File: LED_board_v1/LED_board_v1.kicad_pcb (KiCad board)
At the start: 2 copper layers, 100 x 68 mm, 45 parts, among them J1 Conn_01x03_Pin, J10 Conn_01x03_Pin, J11 Conn_01x03_Pin, J12 Conn_01x02_Pin, J2 Conn_ST_STDC14, J3 Conn_01x03_Pin, J4 Conn_01x03_Pin, J5 Conn_01x03_Pin, J6 Conn_01x03_Pin, J7 Conn_01x03_Pin, J8 Conn_01x03_Pin, J9 Conn_01x03_Pin, SW1 SW_Push, SW2 SW_SPDT, U1 PTCAN3414DDFR, U2 STM32H533CETx, U3 NID60S48-24, U4 BD33FC0FP, U5 74AHCT125, U6 74AHCT125

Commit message: md改良(ちょっと前にしたやつ上げ忘れ)
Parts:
- added D1: LED, LED_SMD:LED_0805_2012Metric_Pad1.15x1.40mm_HandSolder, F.Cu at (105.2, 83.4)
- added D3: LED, LED_SMD:LED_0805_2012Metric_Pad1.15x1.40mm_HandSolder, F.Cu at (109.1, 83.4)
- added R3: 1k, Resistor_SMD:R_0603_1608Metric_Pad0.98x0.95mm_HandSolder, B.Cu at (105.3, 83.4)
- added R4: 1k, Resistor_SMD:R_0603_1608Metric_Pad0.98x0.95mm_HandSolder, B.Cu at (109.1, 83.4)
- moved C14 0.78 mm to (99.5, 84.9)
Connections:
- U2 pad 25: unconnected-(U2-PB12-Pad25) -> Net-(D1-A)
- U2 pad 26: unconnected-(U2-PB13-Pad26) -> Net-(D3-A)
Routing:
- net Net-(D3-A): track 0.00 -> 9.68 mm
- net GND: track 23.0 -> 31.1 mm, vias 68 -> 138
- net Net-(D1-A): track 0.00 -> 5.66 mm
- net nrst: track 36.4 -> 38.6 mm
- net +3.3V: track 87.1 -> 86.6 mm
- net Net-(D3-K): track 0.00 -> 0.13 mm, vias 0 -> 1
- net Net-(D1-K): track 0.00 -> 0.05 mm, vias 0 -> 1
- net /can_-: vias 1 -> 2

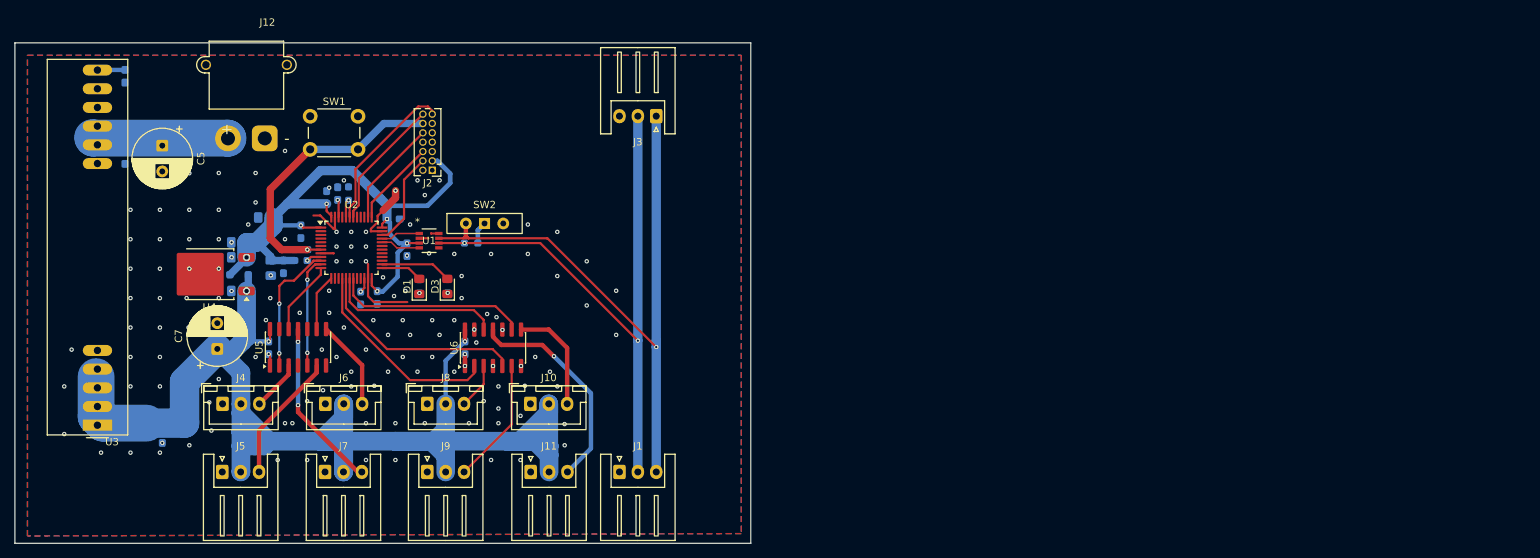
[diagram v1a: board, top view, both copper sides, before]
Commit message: MDPID基板を作ったりLED基板の電源回りをいじった
MDPIDの電源変更+配線
LED基板の電源変更(未配線)
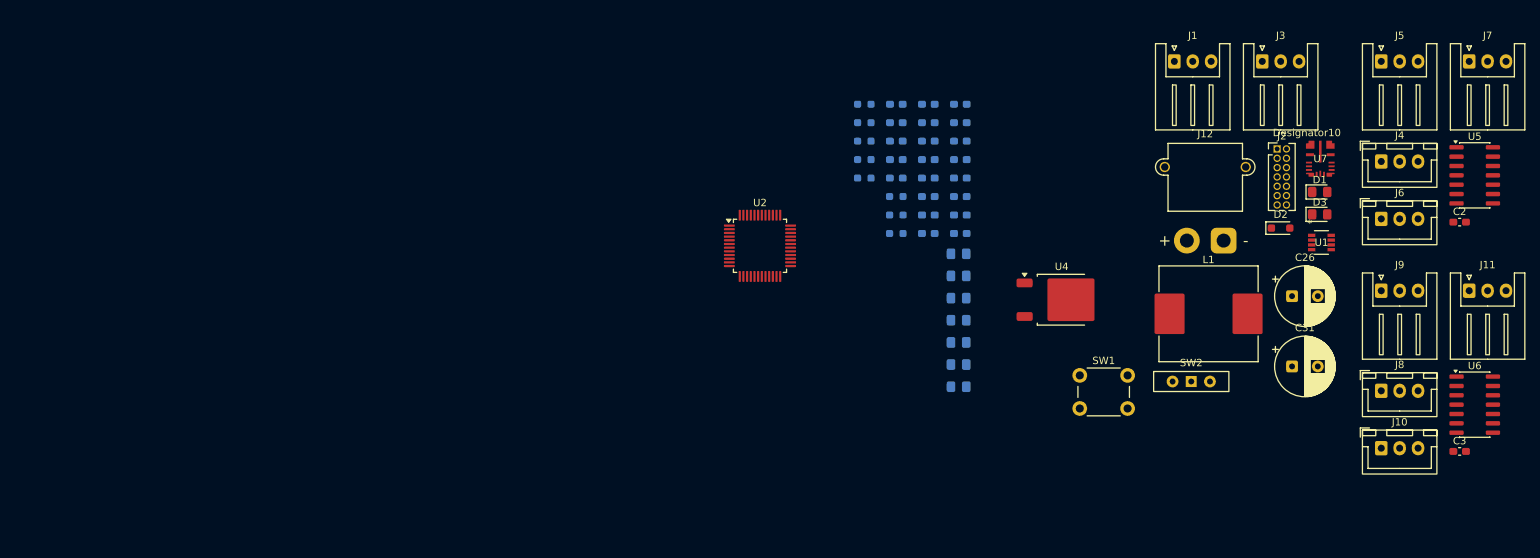
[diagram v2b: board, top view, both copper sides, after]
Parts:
- removed C4, C6, C8: 0.1uF, Capacitor_SMD:C_0603_1608Metric_Pad1.08x0.95mm_HandSolder
- removed C5, C7: 100uF, Capacitor_THT:CP_Radial_D8.0mm_P3.50mm
- removed U3: NID60S48-24, Converter_DCDC:Converter_DCDC_MeanWell_NID60_THT
- added C22: 0.47uF, Capacitor_SMD:C_0603_1608Metric_Pad1.08x0.95mm_HandSolder, B.Cu at (174.4, 61.2)
- added C23: 10μF, Capacitor_SMD:C_0805_2012Metric_Pad1.18x1.45mm_HandSolder, B.Cu at (178.5, 94.0)
- added C24: 10μF, Capacitor_SMD:C_0805_2012Metric_Pad1.18x1.45mm_HandSolder, B.Cu at (178.5, 97.0)
- added C25: 0.47uF, Capacitor_SMD:C_0603_1608Metric_Pad1.08x0.95mm_HandSolder, B.Cu at (174.4, 63.7)
- added C26: 100uF, Capacitor_THT:CP_Radial_D8.0mm_P3.50mm, F.Cu at (223.8, 84.7)
- added C27: 15pF, Capacitor_SMD:C_0603_1608Metric_Pad1.08x0.95mm_HandSolder, B.Cu at (174.4, 66.2)
- added C28: 22uF, Capacitor_SMD:C_0603_1608Metric_Pad1.08x0.95mm_HandSolder, B.Cu at (174.4, 68.7)
- added C29: 0.1uF, Capacitor_SMD:C_0603_1608Metric_Pad1.08x0.95mm_HandSolder, B.Cu at (174.4, 71.2)
- added C30: 1uF, Capacitor_SMD:C_0603_1608Metric_Pad1.08x0.95mm_HandSolder, B.Cu at (174.4, 73.7)
- added C31: 100uF, Capacitor_THT:CP_Radial_D8.0mm_P3.50mm, F.Cu at (223.8, 94.3)
- added C32: 22uF, Capacitor_SMD:C_0603_1608Metric_Pad1.08x0.95mm_HandSolder, B.Cu at (174.4, 76.2)
- added C33: 22uF, Capacitor_SMD:C_0603_1608Metric_Pad1.08x0.95mm_HandSolder, B.Cu at (170.1, 58.6)
- added C34: 22uF, Capacitor_SMD:C_0603_1608Metric_Pad1.08x0.95mm_HandSolder, B.Cu at (170.1, 61.2)
- added C35: 22uF, Capacitor_SMD:C_0603_1608Metric_Pad1.08x0.95mm_HandSolder, B.Cu at (170.1, 63.7)
- added C36: 0.1uF, Capacitor_SMD:C_0603_1608Metric_Pad1.08x0.95mm_HandSolder, B.Cu at (170.1, 66.2)
- added L1: 2.7uH, Inductor_SMD:L_APV_APH1250, F.Cu at (212.5, 87.1)
- added R5: 4.99k, Resistor_SMD:R_0603_1608Metric_Pad0.98x0.95mm_HandSolder, B.Cu at (165.7, 61.2)
- added R6: 10k, Resistor_SMD:R_0603_1608Metric_Pad0.98x0.95mm_HandSolder, B.Cu at (165.7, 63.7)
- added R7: 100k, Resistor_SMD:R_0603_1608Metric_Pad0.98x0.95mm_HandSolder, B.Cu at (165.7, 66.2)
- added R8: 24.9k, Resistor_SMD:R_0603_1608Metric_Pad0.98x0.95mm_HandSolder, B.Cu at (165.7, 68.7)
- added U7: LM61495RPHR, LM61495:RPH0016A, F.Cu at (227.7, 66.1)
- C2, C3, D2: moved to F.Cu
- moved J5 167.1 mm to (236.0, 52.8)
- moved J7 165.2 mm to (247.9, 52.8)
- moved C2 162.7 mm to (246.6, 74.7), turned to 0 degrees
- moved U5 161.6 mm to (248.7, 68.3), turned to 0 degrees
- moved J4 160.9 mm to (236.0, 66.4)
- moved J6 145.7 mm to (236.0, 74.2)
- moved D2 141.7 mm to (222.3, 75.5), turned to 0 degrees
- moved C3 135.9 mm to (246.6, 105.8), turned to 0 degrees
- moved U6 133.6 mm to (248.7, 99.5), turned to 0 degrees
- moved J9 132.0 mm to (236.0, 84.0)
- moved J12 131.0 mm to (214.6, 77.2)
- moved J11 129.9 mm to (247.9, 84.0)
- moved J8 129.7 mm to (236.0, 97.6)
- moved D1 123.0 mm to (227.6, 70.6), turned to 0 degrees
- moved U1 121.3 mm to (227.8, 77.4)
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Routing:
- net +5V: track 191.4 -> 0.00 mm, vias 3 -> 0
- net /can_+: track 87.1 -> 0.00 mm, vias 1 -> 0
- net +3.3V: track 86.6 -> 0.00 mm, vias 6 -> 0
- net /can_-: track 80.9 -> 0.00 mm, vias 2 -> 0
- net nrst: track 38.6 -> 0.00 mm, vias 1 -> 0
- net GND: track 31.1 -> 0.00 mm, vias 138 -> 0
- net Net-(J11-Pin_3): track 29.5 -> 0.00 mm, vias 1 -> 0
- net /tapeled_6: track 29.1 -> 0.00 mm
- net /tapeled_5: track 27.7 -> 0.00 mm
- net /tapeled_8: track 26.3 -> 0.00 mm
- net /tapeled_7: track 23.7 -> 0.00 mm
- net Net-(J7-Pin_3): track 23.3 -> 0.00 mm, vias 2 -> 0
- net strx: track 21.5 -> 0.00 mm
- net +24V: track 18.5 -> 0.00 mm
- net /tapeled_1: track 17.9 -> 0.00 mm, vias 2 -> 0
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- removed copper zone on B.Cu, net GND
- removed copper zone on F.Cu, net GND
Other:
- board outline removed
